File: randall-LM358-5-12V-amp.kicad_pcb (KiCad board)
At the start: 2 copper layers, 100.3 x 77.5 mm, 28 parts, among them J1 Power, M1 Fan_3pin, M2 Fan_3pin, Q1 TIP120, Q2 TIP120, U1 LM2674M-3.3, U2 LM358, U3 Z-Uno-Module

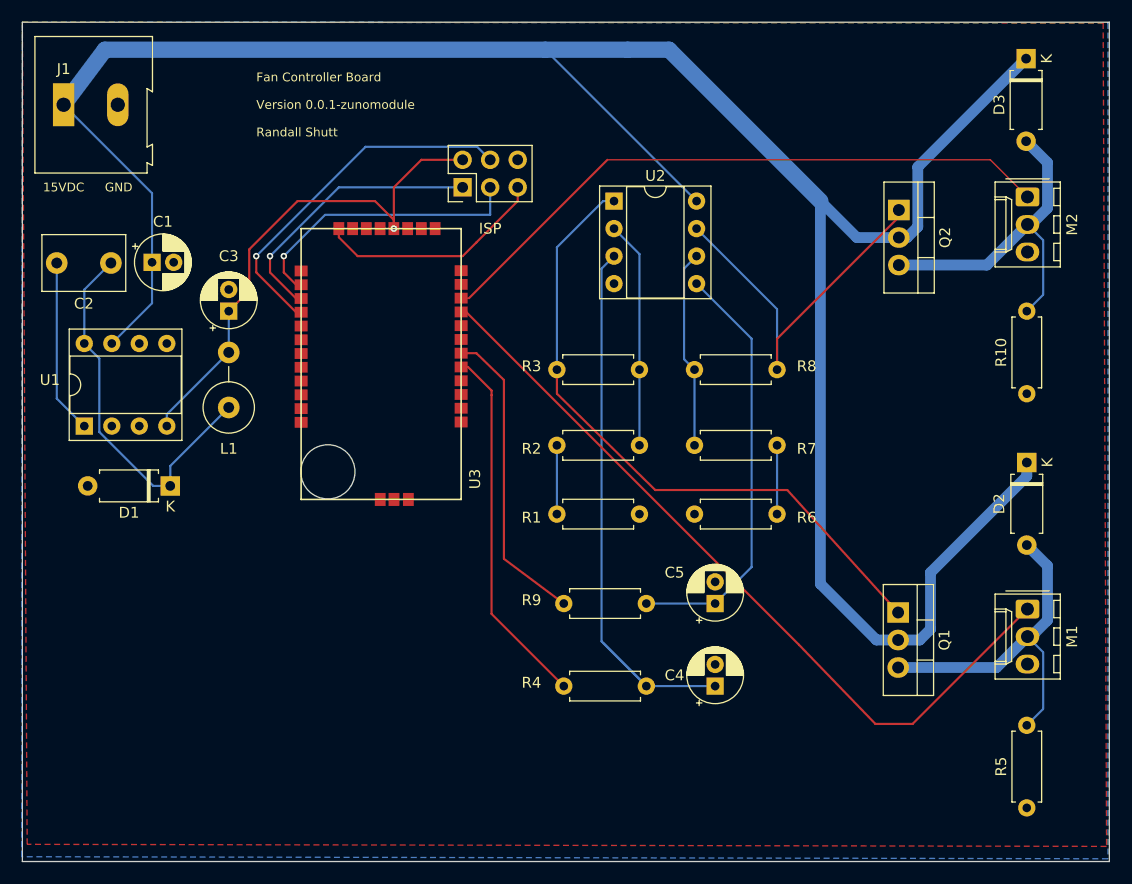
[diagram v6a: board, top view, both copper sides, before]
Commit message: added drill holes and re-arrange board
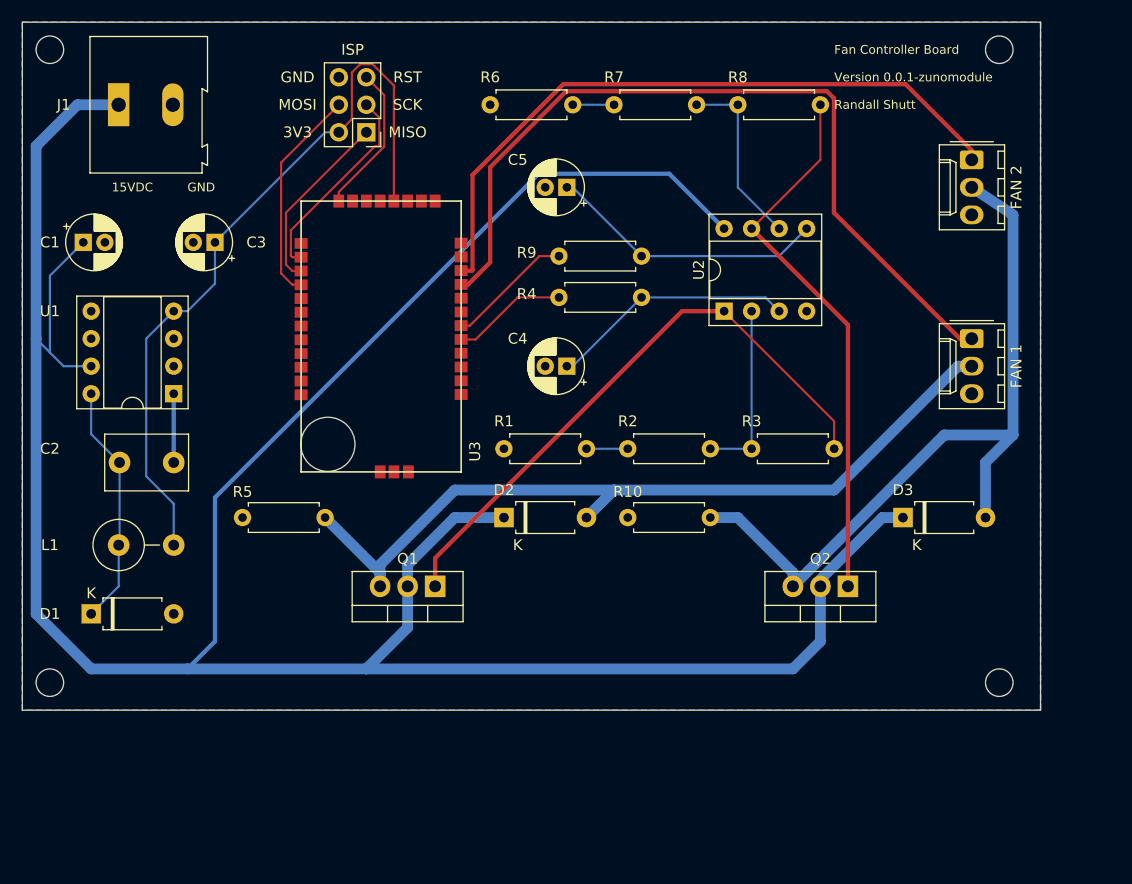
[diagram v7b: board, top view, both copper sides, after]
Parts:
- FAN 1: renamed from M1
- FAN 2: renamed from M2
- Q1, Q2: footprint Package_TO_SOT_THT:TO-220-3_Vertical -> Package_TO_SOT_THT:TO-220-3_Vertical_with_heatsink
- moved R5 77.2 mm to (102.9, 105.4), turned to 0 degrees
- moved D2 48.5 mm to (127.0, 105.4), turned to 0 degrees
- moved D3 43.9 mm to (163.8, 105.4), turned to 0 degrees
- moved Q1 42.8 mm to (120.7, 111.8), turned to 180 degrees
- moved R6 42.2 mm to (133.3, 67.3)
- moved C5 40.8 mm to (132.8, 74.9), turned to 180 degrees
- moved R10 38.6 mm to (138.4, 105.4), turned to 0 degrees
- moved R4 35.9 mm to (139.7, 85.1)
- moved Q2 35.1 mm to (158.8, 111.8), turned to 180 degrees
- moved C4 32.5 mm to (132.8, 91.4), turned to 180 degrees
- moved R9 32.1 mm to (139.7, 81.3)
- moved R7 31.4 mm to (144.8, 67.3), turned to 180 degrees
- moved R3 26.6 mm to (157.5, 99.1), turned to 180 degrees
- moved FAN 1 25.5 mm to (170.2, 88.9)
- moved R8 24.8 mm to (156.2, 67.3)
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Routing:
- net Net-(D2-Pad2): track 32.7 -> 76.2 mm
- net Net-(D3-Pad2): track 32.1 -> 70.7 mm
- net 15VDC: track 223.0 -> 261.4 mm
- net Net-(C4-Pad1): track 53.9 -> 22.7 mm
- net PWM1: track 33.8 -> 10.6 mm
- net 3V3DC: track 47.4 -> 69.7 mm, vias 1 -> 0
- net PWM2: track 28.4 -> 11.7 mm
- net Net-(Q2-Pad1): track 35.5 -> 50.8 mm
- net Net-(C5-Pad1): track 39.4 -> 25.8 mm
- net MOSI: track 33.4 -> 20.1 mm, vias 1 -> 0
- net Net-(C2-Pad1): track 35.3 -> 22.5 mm
- net Net-(C2-Pad2): track 16.1 -> 6.35 mm
- net MISO: track 25.8 -> 16.9 mm, vias 1 -> 0
- net SCK: track 26.7 -> 19.0 mm, vias 1 -> 0
- net RST: track 21.4 -> 13.8 mm
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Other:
- board size 100.3 x 77.5 mm -> 94 x 63.5 mm

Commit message: version number
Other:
- board text added: "Version 0.0.2-zunomodule"
- board text removed: "Version 0.0.1-zunomodule"
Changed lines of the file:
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@@
     (effects (font (size 0.8128 0.8128) (thickness 0.1524)) (justify left))
   )
-  (gr_text "Version 0.0.1-zunomodule" (at 157.48 64.77) (layer F.SilkS)
+  (gr_text "Version 0.0.2-zunomodule" (at 157.48 64.77) (layer F.SilkS)
     (effects (font (size 0.8128 0.8128) (thickness 0.1524)) (justify left))
   )
